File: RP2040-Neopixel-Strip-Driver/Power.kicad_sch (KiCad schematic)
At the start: 15 parts

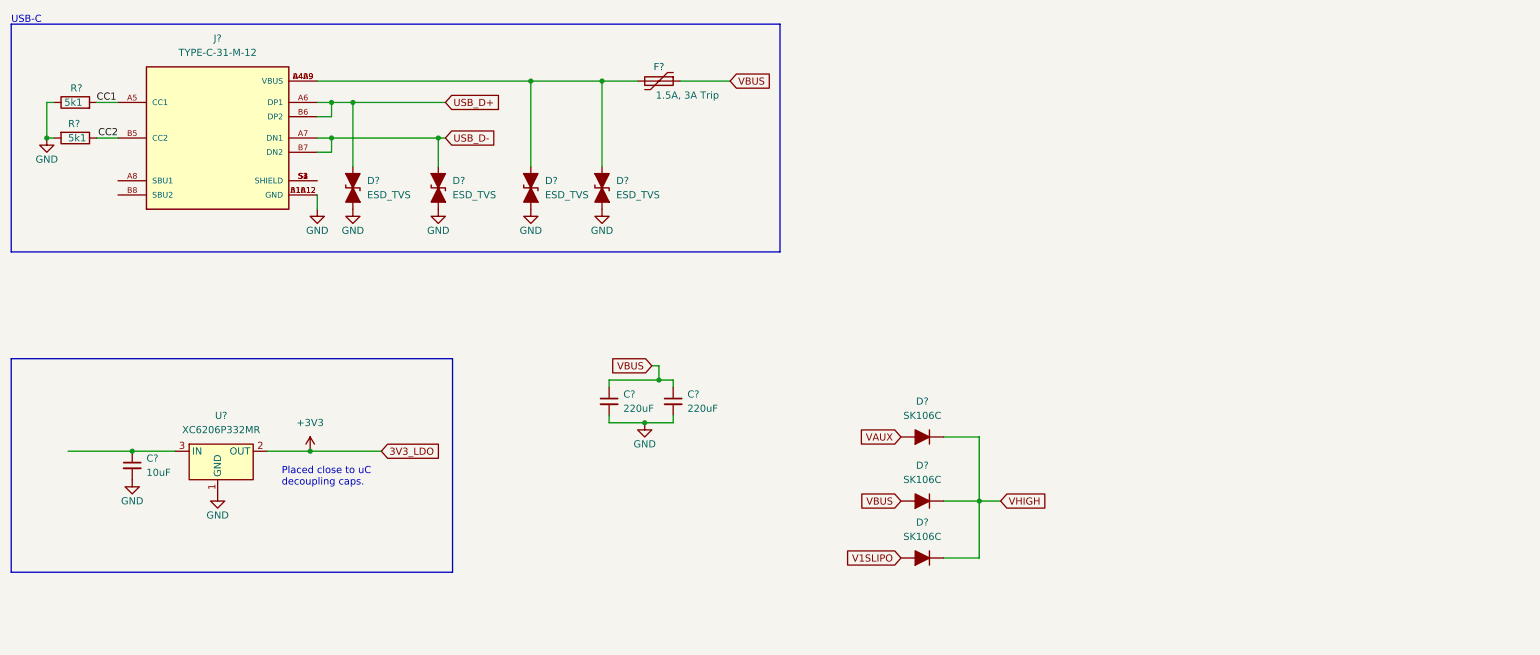
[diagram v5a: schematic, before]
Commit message: Added buck converter IC
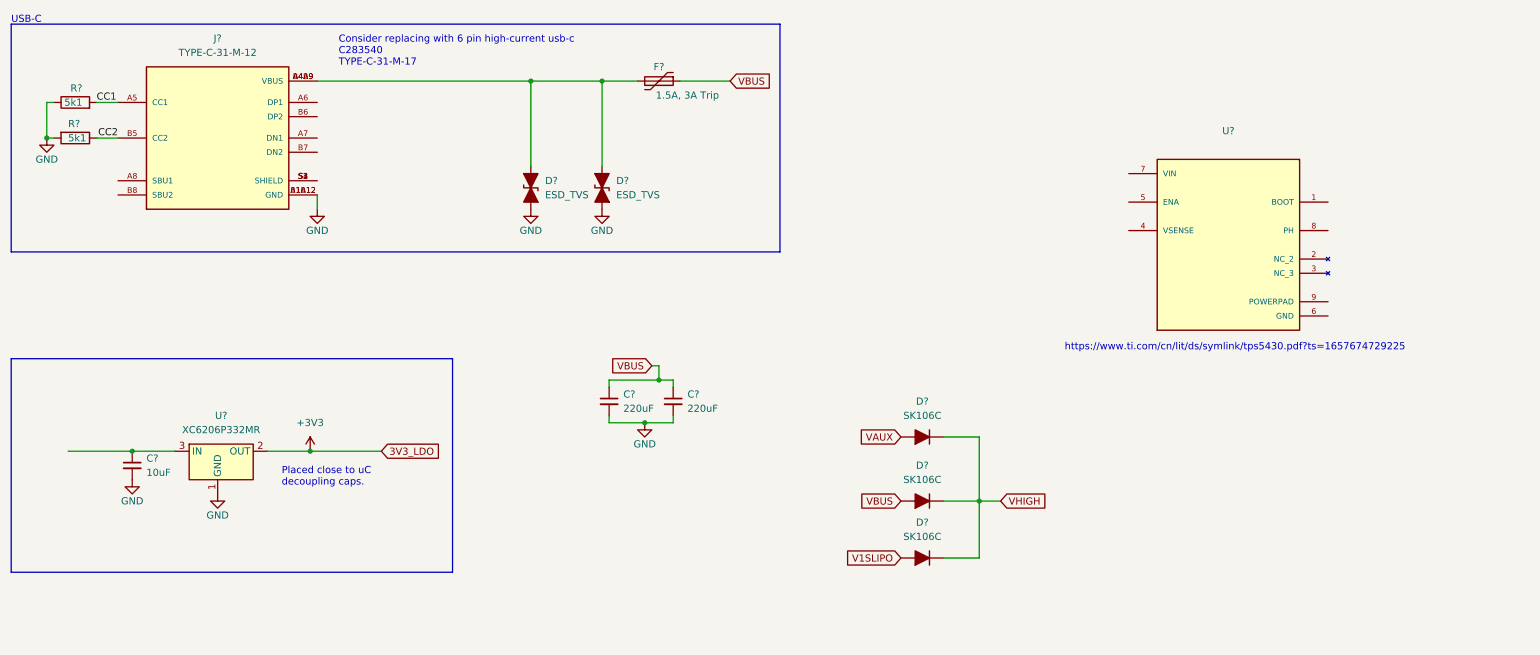
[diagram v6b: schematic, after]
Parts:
- removed D? (x2): ESD_TVS, Breadstick Footprints:Perfect_0402_Resistor, symbol Device:D_TVS_Filled
- added U?: (no value), symbol TPS5430DDAR:TPS5430DDAR
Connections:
- net USB_D+: no longer names the net of J?.A6 (DP1)
- net USB_D+: no longer J?.B6 (DP2)
- net USB_D-: no longer names the net of J?.A7 (DN1)
- net USB_D-: no longer J?.B7 (DN2)
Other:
- note added: "Consider replacing with 6 pin high-current usb-c C283540 TYPE-C-31-M-17"
- note added: "https://www.ti.com/cn/lit/ds/symlink/tps5430.pdf?ts=1657674729225"
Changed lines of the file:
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@@
 (kicad_sch (version 20211123) (generator eeschema)
   (paper "A4")
-  (junction (at 91.44 38.1) (diameter 0) (color 0 0 0 0)
-  )
   (junction (at 130.81 81.28) (diameter 0) (color 0 0 0 0)
   )
@@
   (junction (at 68.58 93.98) (diameter 0) (color 0 0 0 0)
   )
-  (junction (at 72.39 38.1) (diameter 0) (color 0 0 0 0)
-  )
   (junction (at 36.83 93.98) (diameter 0) (color 0 0 0 0)
   )
-  (junction (at 76.2 31.75) (diameter 0) (color 0 0 0 0)
-  )
   (junction (at 120.65 27.94) (diameter 0) (color 0 0 0 0)
   )
-  (junction (at 72.39 31.75) (diameter 0) (color 0 0 0 0)
-  )
   (junction (at 107.95 27.94) (diameter 0) (color 0 0 0 0)
   )
@@
     (stroke (width 0) (type default) (color 0 0 0 0))
   )
-  (wire (pts (xy 76.2 31.75) (xy 76.2 43.18))
-    (stroke (width 0) (type default) (color 0 0 0 0))
-  )
-  (wire (pts (xy 72.39 31.75) (xy 76.2 31.75))
-    (stroke (width 0) (type default) (color 0 0 0 0))
-  )
-  (wire (pts (xy 72.39 40.64) (xy 72.39 38.1))
-    (stroke (width 0) (type default) (color 0 0 0 0))
-  )
   (polyline (pts (xy 15.24 115.57) (xy 93.98 115.57))
     (stroke (width 0) (type default) (color 0 0 0 0))
@@
     (stroke (width 0) (type default) (color 0 0 0 0))
   )
-  (wire (pts (xy 91.44 38.1) (xy 92.71 38.1))
-    (stroke (width 0) (type default) (color 0 0 0 0))
-  )
   (wire (pts (xy 107.95 27.94) (xy 107.95 43.18))
     (stroke (width 0) (type default) (color 0 0 0 0))
@@
     (stroke (width 0) (type default) (color 0 0 0 0))
   )
-  (wire (pts (xy 72.39 38.1) (xy 91.44 38.1))
-    (stroke (width 0) (type default) (color 0 0 0 0))
-  )
-  (wire (pts (xy 72.39 31.75) (xy 69.85 31.75))
-    (stroke (width 0) (type default) (color 0 0 0 0))
-  )
   (wire (pts (xy 69.85 27.94) (xy 107.95 27.94))
     (stroke (width 0) (type default) (color 0 0 0 0))
@@
     (stroke (width 0) (type default) (color 0 0 0 0))
   )
-  (wire (pts (xy 72.39 34.29) (xy 72.39 31.75))
-    (stroke (width 0) (type default) (color 0 0 0 0))
-  )
   (wire (pts (xy 133.35 81.28) (xy 133.35 82.55))
     (stroke (width 0) (type default) (color 0 0 0 0))
@@
     (stroke (width 0) (type default) (color 0 0 0 0))
   )
-  (wire (pts (xy 91.44 38.1) (xy 91.44 43.18))
-    (stroke (width 0) (type default) (color 0 0 0 0))
-  )
   (wire (pts (xy 36.83 93.98) (xy 44.45 93.98))
     (stroke (width 0) (type default) (color 0 0 0 0))
@@
     (stroke (width 0) (type default) (color 0 0 0 0))
   )
-  (wire (pts (xy 69.85 40.64) (xy 72.39 40.64))
-    (stroke (width 0) (type default) (color 0 0 0 0))
-  )
   (wire (pts (xy 133.35 87.63) (xy 133.35 88.9))
     (stroke (width 0) (type default) (color 0 0 0 0))
@@
     (stroke (width 0) (type default) (color 0 0 0 0))
   )
-  (wire (pts (xy 69.85 34.29) (xy 72.39 34.29))
-    (stroke (width 0) (type default) (color 0 0 0 0))
-  )
   (wire (pts (xy 69.85 48.26) (xy 69.85 50.8))
     (stroke (width 0) (type default) (color 0 0 0 0))
@@
     (stroke (width 0) (type default) (color 0 0 0 0))
   )
-  (wire (pts (xy 72.39 38.1) (xy 69.85 38.1))
-    (stroke (width 0) (type default) (color 0 0 0 0))
-  )
   (wire (pts (xy 129.54 78.74) (xy 130.81 78.74))
     (stroke (width 0) (type default) (color 0 0 0 0))
@@
     (stroke (width 0) (type default) (color 0 0 0 0))
   )
-  (wire (pts (xy 76.2 31.75) (xy 92.71 31.75))
-    (stroke (width 0) (type default) (color 0 0 0 0))
-  )
   (polyline (pts (xy 15.24 77.47) (xy 93.98 77.47))
     (stroke (width 0) (type default) (color 0 0 0 0))
@@
   )
   (text "Placed close to uC \ndecoupling caps." (at 63.5 100.33 0)
+    (effects (font (size 1.27 1.27)) (justify left bottom))
+  )
+  (text "Consider replacing with 6 pin high-current usb-c \nC283540\nTYPE-C-31-M-17"
+    (at 73.66 25.4 0)
+    (effects (font (size 1.27 1.27)) (justify left bottom))
+  )
+  (text "https://www.ti.com/cn/lit/ds/symlink/tps5430.pdf?ts=1657674729225"
+    (at 203.2 76.2 0)
     (effects (font (size 1.27 1.27)) (justify left bottom))
   )
@@
     )
   )
-  (global_label "USB_D+" (shape input) (at 92.71 31.75 0) (fields_autoplaced)
-    (effects (font (size 1.27 1.27)) (justify left))
-    (property "Intersheet References" "${INTERSHEET_REFS}" (id 0) (at 102.7431 31.6706 0)
-      (effects (font (size 1.27 1.27)) (justify left) hide)
-    )
-  )
   (global_label "VBUS" (shape input) (at 129.54 78.74 180) (fields_autoplaced)
     (effects (font (size 1.27 1.27)) (justify right))
@@
     )
   )
-  (global_label "USB_D-" (shape input) (at 92.71 38.1 0) (fields_autoplaced)
-    (effects (font (size 1.27 1.27)) (justify left))
-    (property "Intersheet References" "${INTERSHEET_REFS}" (id 0) (at 102.7431 38.0206 0)
-      (effects (font (size 1.27 1.27)) (justify left) hide)
-    )
-  )
   (global_label "VBUS" (shape input) (at 143.51 27.94 0) (fields_autoplaced)
     (effects (font (size 1.27 1.27)) (justify left))
@@
     (pin "1")
   )
-  (symbol (lib_id "power:GND") (at 91.44 50.8 0) (unit 1)
-    (in_bom yes) (on_board yes)
-    (property "Reference" "#PWR?" (id 0) (at 91.44 57.15 0)
-      (effects (font (size 1.27 1.27)) hide)
-    )
-    (property "Value" "GND" (id 1) (at 91.44 54.61 0))
-    (property "Footprint" "" (id 2) (at 91.44 50.8 0)
-      (effects (font (size 1.27 1.27)) hide)
-    )
-    (property "Datasheet" "" (id 3) (at 91.44 50.8 0)
-      (effects (font (size 1.27 1.27)) hide)
-    )
-    (pin "1")
-  )
   (symbol (lib_id "Device:D_Filled") (at 177.8 91.44 180) (unit 1)
     (in_bom yes) (on_board yes) (fields_autoplaced)
@@
     (pin "2")
   )
+  (symbol (lib_id "TPS5430DDAR:TPS5430DDAR") (at 232.41 57.15 0) (unit 1)
+    (in_bom yes) (on_board yes) (fields_autoplaced)
+    (property "Reference" "U?" (id 0) (at 232.41 36.83 0))
+    (property "Value" "" (id 1) (at 232.41 39.37 0))
+    (property "Footprint" "" (id 2) (at 232.41 57.15 0)
+      (effects (font (size 1.27 1.27)) (justify left bottom) hide)
+    )
+    (property "Datasheet" "" (id 3) (at 232.41 57.15 0)
+      (effects (font (size 1.27 1.27)) (justify left bottom) hide)
+    )
+    (property "PARTREV" "I" (id 4) (at 232.41 57.15 0)
+      (effects (font (size 1.27 1.27)) (justify left bottom) hide)
+    )
+    (property "MANUFACTURER" "Texas Instruments" (id 5) (at 232.41 57.15 0)
+      (effects (font (size 1.27 1.27)) (justify left bottom) hide)
+    )
+    (property "MAXIMUM_PACKAGE_HEIGHT" "1.70 mm" (id 6) (at 232.41 57.15 0)
+      (effects (font (size 1.27 1.27)) (justify left bottom) hide)
+    )
+    (property "STANDARD" "Manufacturer Recommendations" (id 7) (at 232.41 57.15 0)
+      (effects (font (size 1.27 1.27)) (justify left bottom) hide)
+    )
+    (property "JLCPCB P/N" "C9864" (id 8) (at 232.41 57.15 0)
+      (effects (font (size 1.27 1.27)) hide)
+    )
+    (pin "1")
+    (pin "2")
+    (pin "3")
+    (pin "4")
+    (pin "5")
+    (pin "6")
+    (pin "7")
+    (pin "8")
+    (pin "9")
+  )
   (symbol (lib_id "Device:D_TVS_Filled") (at 120.65 46.99 90) (unit 1)
     (in_bom yes) (on_board yes) (fields_autoplaced)
@@
     )
     (property "JLCPCB P/N" "C316049" (id 4) (at 120.65 46.99 0)
-      (effects (font (size 1.27 1.27)) hide)
-    )
-    (pin "1")
-    (pin "2")
-  )
-  (symbol (lib_id "Device:D_TVS_Filled") (at 91.44 46.99 90) (unit 1)
-    (in_bom yes) (on_board yes) (fields_autoplaced)
-    (property "Reference" "D?" (id 0) (at 93.98 45.7199 90)
-      (effects (font (size 1.27 1.27)) (justify right))
-    )
-    (property "Value" "ESD_TVS" (id 1) (at 93.98 48.2599 90)
-      (effects (font (size 1.27 1.27)) (justify right))
-    )
-    (property "Footprint" "Breadstick Footprints:Perfect_0402_Resistor" (id 2) (at 91.44 46.99 0)
-      (effects (font (size 1.27 1.27)) hide)
-    )
-    (property "Datasheet" "~" (id 3) (at 91.44 46.99 0)
-      (effects (font (size 1.27 1.27)) hide)
-    )
-    (property "JLCPCB P/N" "C316049" (id 4) (at 91.44 46.99 0)
       (effects (font (size 1.27 1.27)) hide)
     )
@@
     (pin "2")
   )
-  (symbol (lib_id "Device:D_TVS_Filled") (at 76.2 46.99 90) (unit 1)
-    (in_bom yes) (on_board yes)
-    (property "Reference" "D?" (id 0) (at 78.74 45.7199 90)
-      (effects (font (size 1.27 1.27)) (justify right))
-    )
-    (property "Value" "ESD_TVS" (id 1) (at 78.74 48.2599 90)
-      (effects (font (size 1.27 1.27)) (justify right))
-    )
-    (property "Footprint" "Breadstick Footprints:Perfect_0402_Resistor" (id 2) (at 76.2 46.99 0)
-      (effects (font (size 1.27 1.27)) hide)
-    )
-    (property "Datasheet" "~" (id 3) (at 76.2 46.99 0)
-      (effects (font (size 1.27 1.27)) hide)
-    )
-    (property "JLCPCB P/N" "C316049" (id 4) (at 76.2 46.99 0)
-      (effects (font (size 1.27 1.27)) hide)
-    )
-    (pin "1")
-    (pin "2")
-  )
-  (symbol (lib_id "power:GND") (at 76.2 50.8 0) (unit 1)
-    (in_bom yes) (on_board yes)
-    (property "Reference" "#PWR?" (id 0) (at 76.2 57.15 0)
-      (effects (font (size 1.27 1.27)) hide)
-    )
-    (property "Value" "GND" (id 1) (at 76.2 54.61 0))
-    (property "Footprint" "" (id 2) (at 76.2 50.8 0)
-      (effects (font (size 1.27 1.27)) hide)
-    )
-    (property "Datasheet" "" (id 3) (at 76.2 50.8 0)
-      (effects (font (size 1.27 1.27)) hide)
-    )
-    (pin "1")
-  )
   (symbol (lib_id "power:GND") (at 36.83 99.06 0) (unit 1)
